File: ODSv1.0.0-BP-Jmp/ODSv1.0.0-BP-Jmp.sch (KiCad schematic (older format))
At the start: 4 parts

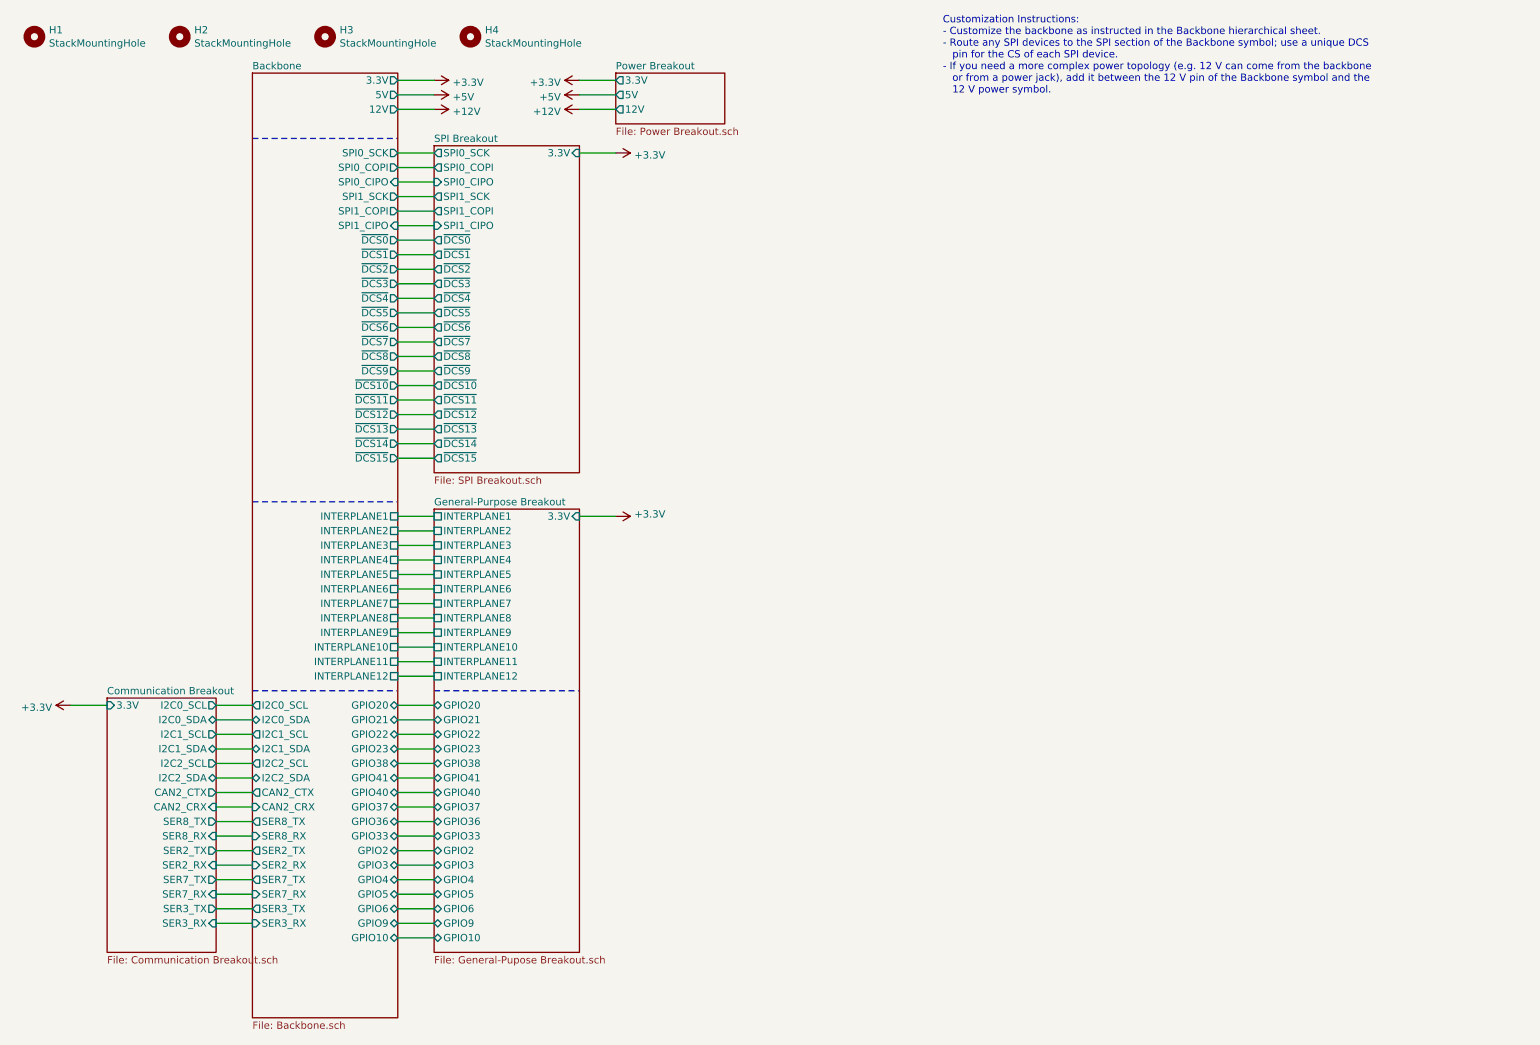
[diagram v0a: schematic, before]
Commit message: Fix hierarchical pin label directions, finish front right corner
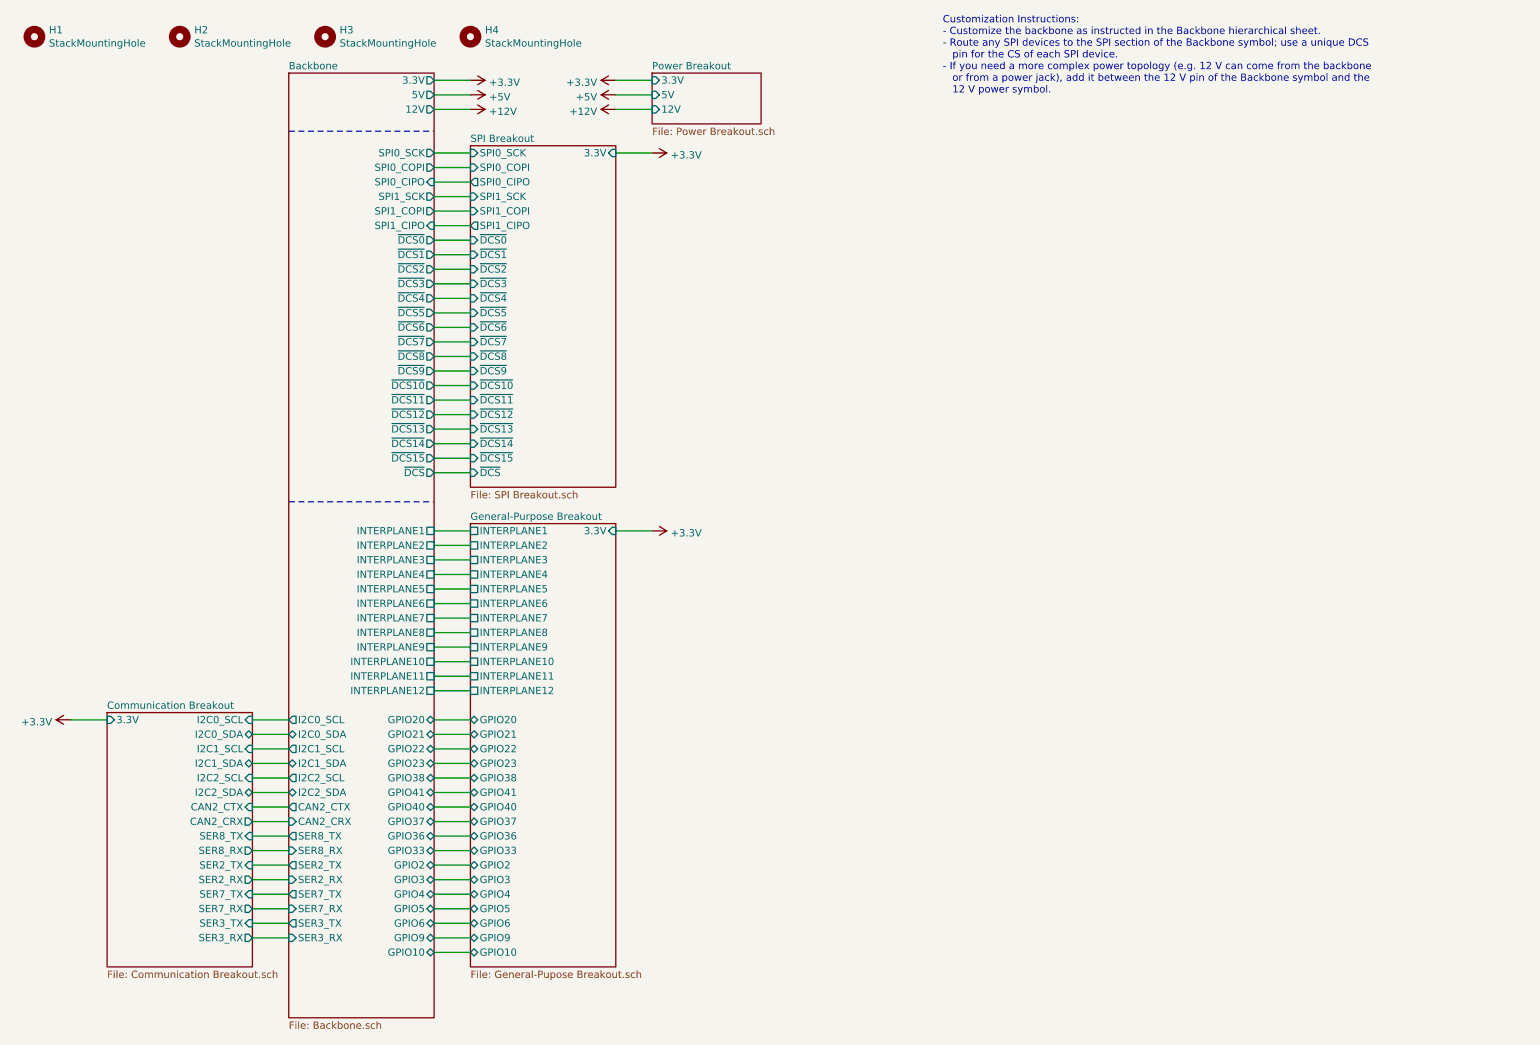
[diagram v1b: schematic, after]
